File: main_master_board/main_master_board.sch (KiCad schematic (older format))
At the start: 22 parts, among them P1 Hebi_1, P13 CONN_02X15, P15 CONN_02X15, P2 Hebi_2, P3 Vbackup, P4 CONN_02X05, P5 Mounting Holes, P6 Mounting Holes, P7 Mounting Holes, P8 Mounting Holes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

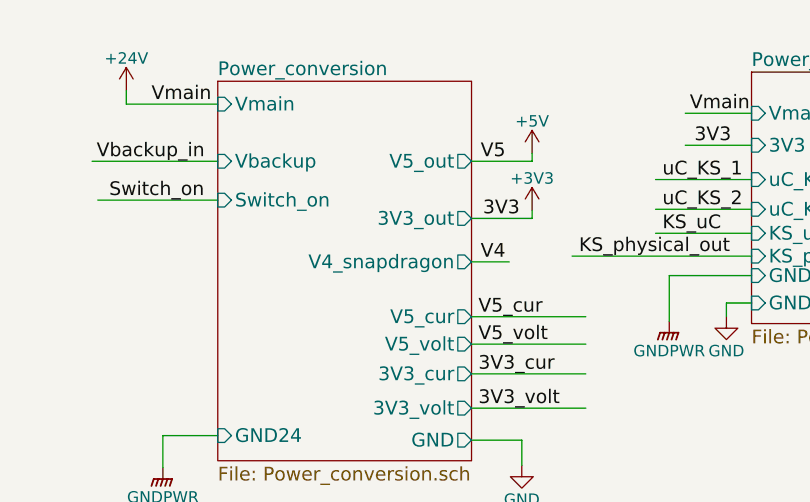
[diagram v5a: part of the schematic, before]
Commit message: Placed all compnenets on board. Now need to route!
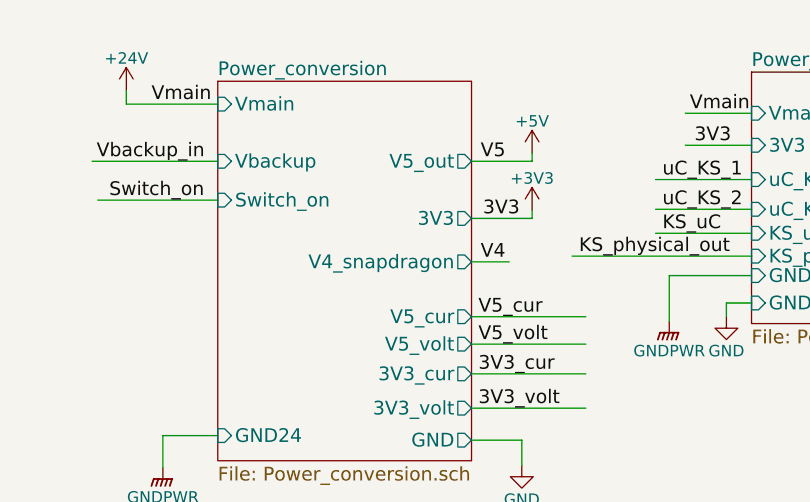
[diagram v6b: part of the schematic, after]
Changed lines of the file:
@@
 LIBS:Sensors
 LIBS:LP3852-3.3
-LIBS:decaWave
+LIBS:0s102011ma1qn1
+LIBS:74LVC1G17
+LIBS:74V1T126
+LIBS:acs711klctr-12ab-t
+LIBS:AD7192
+LIBS:AD7193
+LIBS:am-hrr30-xxx
+LIBS:aon7528
+LIBS:AP7363
+LIBS:AS1359
+LIBS:csd16323q3
+LIBS:dmn2004dmk
+LIBS:dp_devices
+LIBS:DSPIC33E128MC506
+LIBS:fds6898az
+LIBS:ina197
+LIBS:irf7329pbf
+LIBS:ld1117
+LIBS:lm3478
+LIBS:lm3481
+LIBS:lt1910
+LIBS:ltc1871
+LIBS:ltc1982
+LIBS:MAG3110
+LIBS:mcp1700
+LIBS:mcp73831
+LIBS:mcsmt-g5030a1-3712
+LIBS:microchip_can
+LIBS:microclasp_hdrx2
+LIBS:microclasp_hdrx3
+LIBS:MPU-6000_MPU-6050
+LIBS:MPU-9150
+LIBS:nrf24l01+
+LIBS:pds1040l
+LIBS:pic12f1571
+LIBS:pinhead
+LIBS:psmn013-80ys
+LIBS:RESISTOR_ARRAY
+LIBS:rf803d
+LIBS:RGB_LED
+LIBS:Si1970DH
+LIBS:sn65hvd232
+LIBS:ssc54
+LIBS:sw_push_4
+LIBS:tc74
+LIBS:TPS2113A
+LIBS:tps54540
+LIBS:vs-mbrb1635pbf
+LIBS:xal5050-562meb
+LIBS:xal6030-182mec
 LIBS:conn_2x50
 LIBS:conn_open_q_x2
@@
 LIBS:ac-dc
 LIBS:actel
-LIBS:allegro
 LIBS:Altera
 LIBS:analog_devices
@@
 LIBS:logo
 LIBS:maxim
-LIBS:mechanical
 LIBS:microchip_dspic33dsc
 LIBS:microchip_pic10mcu
@@
 LIBS:microchip_pic32mcu
 LIBS:motor_drivers
-LIBS:motors
 LIBS:msp430
 LIBS:nordicsemi
@@
 LIBS:ttl_ieee
 LIBS:video
-LIBS:wiznet
 LIBS:Worldsemi
 LIBS:Xicor
-LIBS:zetex
 LIBS:Zilog
 LIBS:conn_2x45
@@
 F1 "Power_conversion.sch" 60
 F2 "V5_out" O R 4110 1110 60
-F3 "3V3_out" O R 4110 1360 60
-F4 "Vmain" I L 3000 860 60
-F5 "Vbackup" I L 3000 1110 60
-F6 "GND24" I L 3000 2310 60
-F7 "V5_cur" O R 4110 1790 60
-F8 "V5_volt" O R 4110 1910 60
-F9 "3V3_cur" O R 4110 2040 60
-F10 "3V3_volt" O R 4110 2190 60
-F11 "GND" O R 4110 2330 60
-F12 "Switch_on" I L 3000 1280 60
-F13 "V4_snapdragon" O R 4110 1550 60
+F3 "Vmain" I L 3000 860 60
+F4 "Vbackup" I L 3000 1110 60
+F5 "GND24" I L 3000 2310 60
+F6 "V5_cur" O R 4110 1790 60
+F7 "V5_volt" O R 4110 1910 60
+F8 "3V3_cur" O R 4110 2040 60
+F9 "3V3_volt" O R 4110 2190 60
+F10 "GND" O R 4110 2330 60
+F11 "Switch_on" I L 3000 1280 60
+F12 "V4_snapdragon" O R 4110 1550 60
+F13 "3V3" O R 4110 1360 60
 $EndSheet
 Text Label 2470 1110 0    60   ~ 0

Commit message: Updated files to support 3d rendering in KiCAD 3D viewer.
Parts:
- P1, P2: footprint Connectors_Molex:Molex_MiniFit-JR-5556-02A_2x01x4.20mm_Straight -> correct_molex:Molex_MiniFit-JR-5556-02A_2x01x4.20mm_Straight
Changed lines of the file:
@@
 LIBS:Sensors
 LIBS:LP3852-3.3
-LIBS:0s102011ma1qn1
-LIBS:74LVC1G17
-LIBS:74V1T126
-LIBS:acs711klctr-12ab-t
-LIBS:AD7192
-LIBS:AD7193
-LIBS:am-hrr30-xxx
-LIBS:aon7528
-LIBS:AP7363
-LIBS:AS1359
-LIBS:csd16323q3
-LIBS:dmn2004dmk
-LIBS:dp_devices
-LIBS:DSPIC33E128MC506
-LIBS:fds6898az
-LIBS:ina197
-LIBS:irf7329pbf
-LIBS:ld1117
-LIBS:lm3478
-LIBS:lm3481
-LIBS:lt1910
-LIBS:ltc1871
-LIBS:ltc1982
-LIBS:MAG3110
-LIBS:mcp1700
-LIBS:mcp73831
-LIBS:mcsmt-g5030a1-3712
-LIBS:microchip_can
-LIBS:microclasp_hdrx2
-LIBS:microclasp_hdrx3
-LIBS:MPU-6000_MPU-6050
-LIBS:MPU-9150
-LIBS:nrf24l01+
-LIBS:pds1040l
-LIBS:pic12f1571
-LIBS:pinhead
-LIBS:psmn013-80ys
-LIBS:RESISTOR_ARRAY
-LIBS:rf803d
-LIBS:RGB_LED
-LIBS:Si1970DH
-LIBS:sn65hvd232
-LIBS:ssc54
-LIBS:sw_push_4
-LIBS:tc74
-LIBS:TPS2113A
-LIBS:tps54540
-LIBS:vs-mbrb1635pbf
-LIBS:xal5050-562meb
-LIBS:xal6030-182mec
+LIBS:decaWave
 LIBS:conn_2x50
 LIBS:conn_open_q_x2
@@
 LIBS:ac-dc
 LIBS:actel
+LIBS:allegro
 LIBS:Altera
 LIBS:analog_devices
@@
 LIBS:logo
 LIBS:maxim
+LIBS:mechanical
 LIBS:microchip_dspic33dsc
 LIBS:microchip_pic10mcu
@@
 LIBS:microchip_pic32mcu
 LIBS:motor_drivers
+LIBS:motors
 LIBS:msp430
 LIBS:nordicsemi
@@
 LIBS:ttl_ieee
 LIBS:video
+LIBS:wiznet
 LIBS:Worldsemi
 LIBS:Xicor
+LIBS:zetex
 LIBS:Zilog
 LIBS:conn_2x45
@@
 F 0 "P1" H 4525 3400 50  0000 C CNN
 F 1 "Hebi_1" V 4625 3250 50  0000 C CNN
-F 2 "Connectors_Molex:Molex_MiniFit-JR-5556-02A_2x01x4.20mm_Straight" H 4525 3250 50  0001 C CNN
+F 2 "correct_molex:Molex_MiniFit-JR-5556-02A_2x01x4.20mm_Straight" H 4525 3250 50  0001 C CNN
 F 3 "" H 4525 3250 50  0000 C CNN
 	1    4525 3250
@@
 F 0 "P2" H 4525 3840 50  0000 C CNN
 F 1 "Hebi_2" V 4625 3690 50  0000 C CNN
-F 2 "Connectors_Molex:Molex_MiniFit-JR-5556-02A_2x01x4.20mm_Straight" H 4525 3690 50  0001 C CNN
+F 2 "correct_molex:Molex_MiniFit-JR-5556-02A_2x01x4.20mm_Straight" H 4525 3690 50  0001 C CNN
 F 3 "" H 4525 3690 50  0000 C CNN
 	1    4525 3690

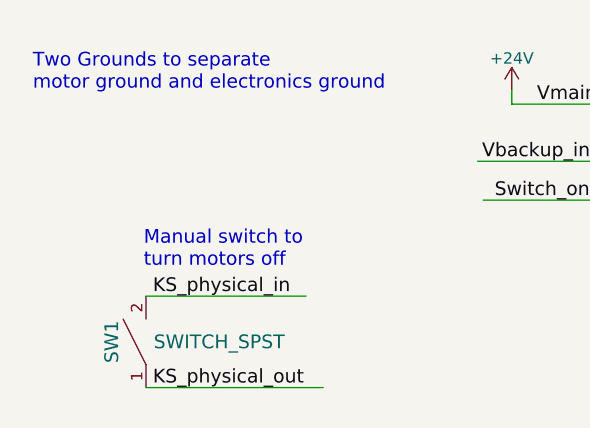
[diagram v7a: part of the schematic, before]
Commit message: Messed up and routed the lan9512 is a bad spot.
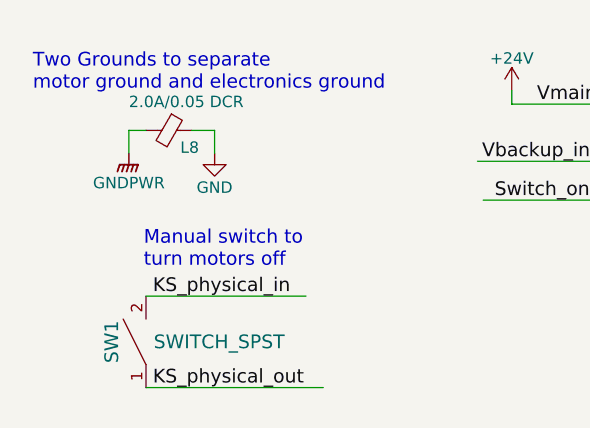
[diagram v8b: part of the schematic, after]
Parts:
- added L8: 2.0A/0.05 DCR, dp_devices2:dp_devices-C603, symbol Ferrite_Bead_Small
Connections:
- wire segments 254 -> 258
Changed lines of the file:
@@
 Text Label 6975 6050 2    60   ~ 0
 USBD3_N
+$Comp
+L Ferrite_Bead_Small L8
+U 1 1 589D34C8
+P 1100 975
+F 0 "L8" V 1175 1025 50  0000 L CNN
+F 1 "2.0A/0.05 DCR" V 975 800 50  0000 L CNN
+F 2 "dp_devices2:dp_devices-C603" V 1030 975 50  0001 C CNN
+F 3 "http://www.digikey.com/product-detail/en/BLM18PG121SN1D/490-1037-1-ND/" H 1100 975 50  0001 C CNN
+	1    1100 975
+	0    1    1    0
+$EndComp
+$Comp
+L GNDPWR #PWR025
+U 1 1 589DB72C
+P 925 1075
+F 0 "#PWR025" H 925 875 50  0001 C CNN
+F 1 "GNDPWR" H 925 945 50  0000 C CNN
+F 2 "" H 925 1025 50  0000 C CNN
+F 3 "" H 925 1025 50  0000 C CNN
+	1    925  1075
+	1    0    0    -1
+$EndComp
+$Comp
+L GND #PWR026
+U 1 1 589DB9F6
+P 1300 1075
+F 0 "#PWR026" H 1300 825 50  0001 C CNN
+F 1 "GND" H 1300 925 50  0000 C CNN
+F 2 "" H 1300 1075 50  0000 C CNN
+F 3 "" H 1300 1075 50  0000 C CNN
+	1    1300 1075
+	1    0    0    -1
+$EndComp
+Wire Wire Line
+	925  1075 925  975
+Wire Wire Line
+	925  975  1000 975
+Wire Wire Line
+	1200 975  1300 975
+Wire Wire Line
+	1300 975  1300 1075
 $EndSCHEMATC
